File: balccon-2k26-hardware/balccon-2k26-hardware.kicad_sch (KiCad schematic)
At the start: 1 part

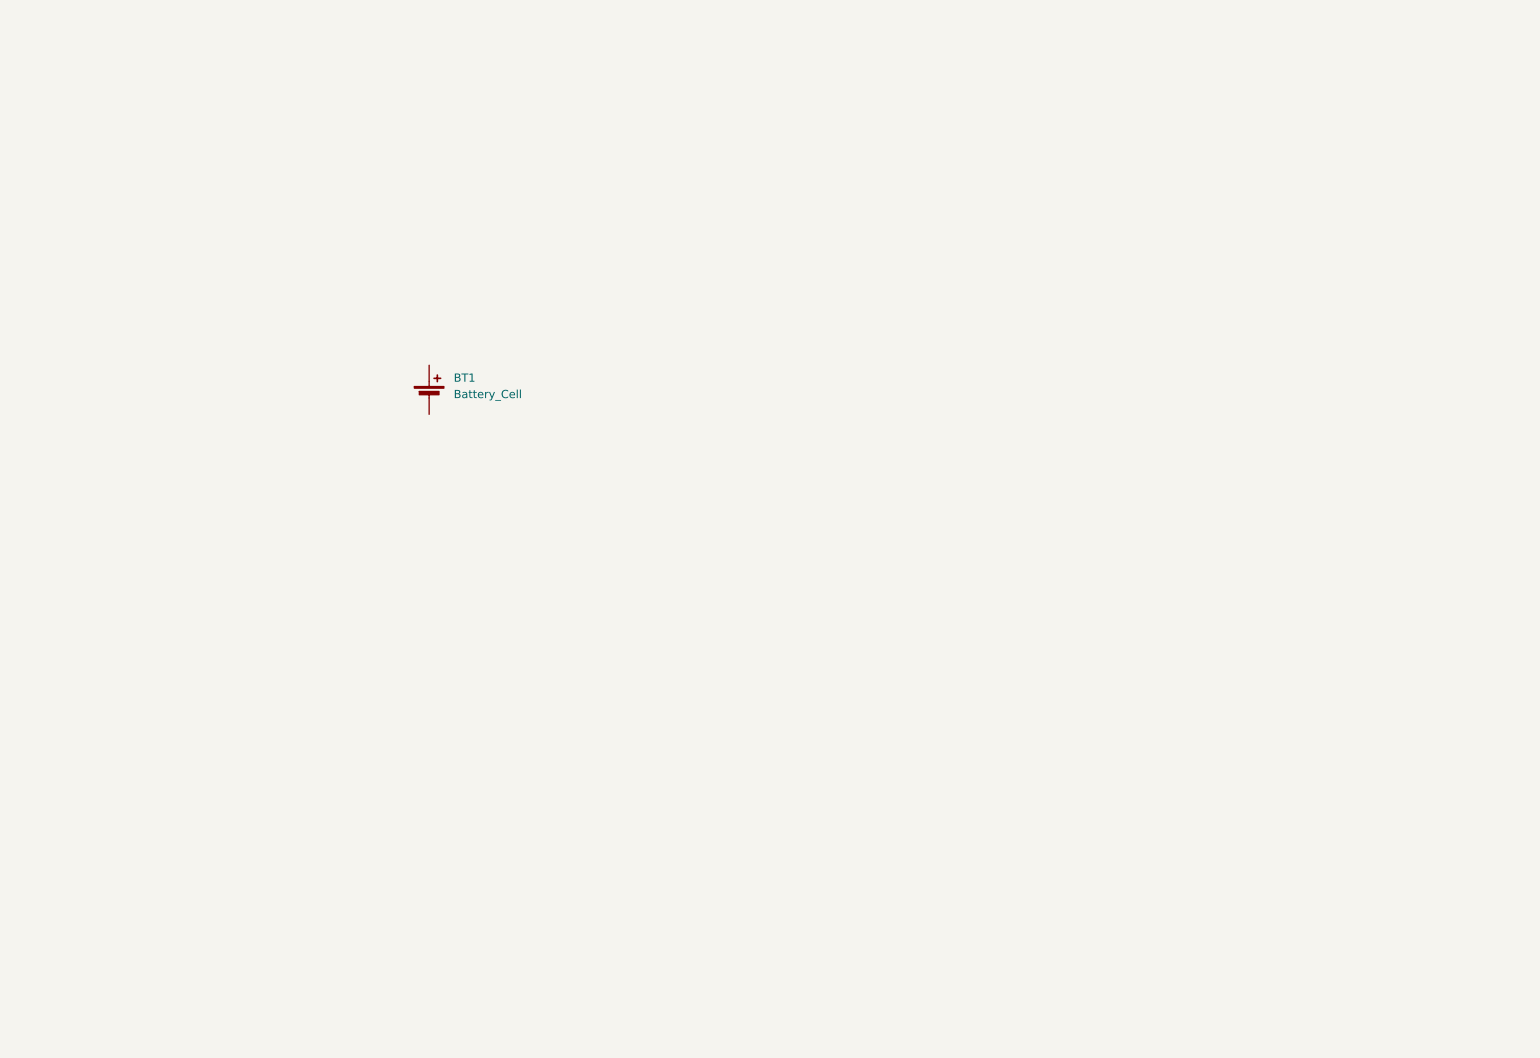
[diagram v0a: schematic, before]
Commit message: Update schematic/board and add hex, log layer exports
Progress the KiCad schematic and board layout, and export the hex and log
layers alongside the existing ones.

Co-Authored-By: Claude Sonnet 5 <noreply@anthropic.com>
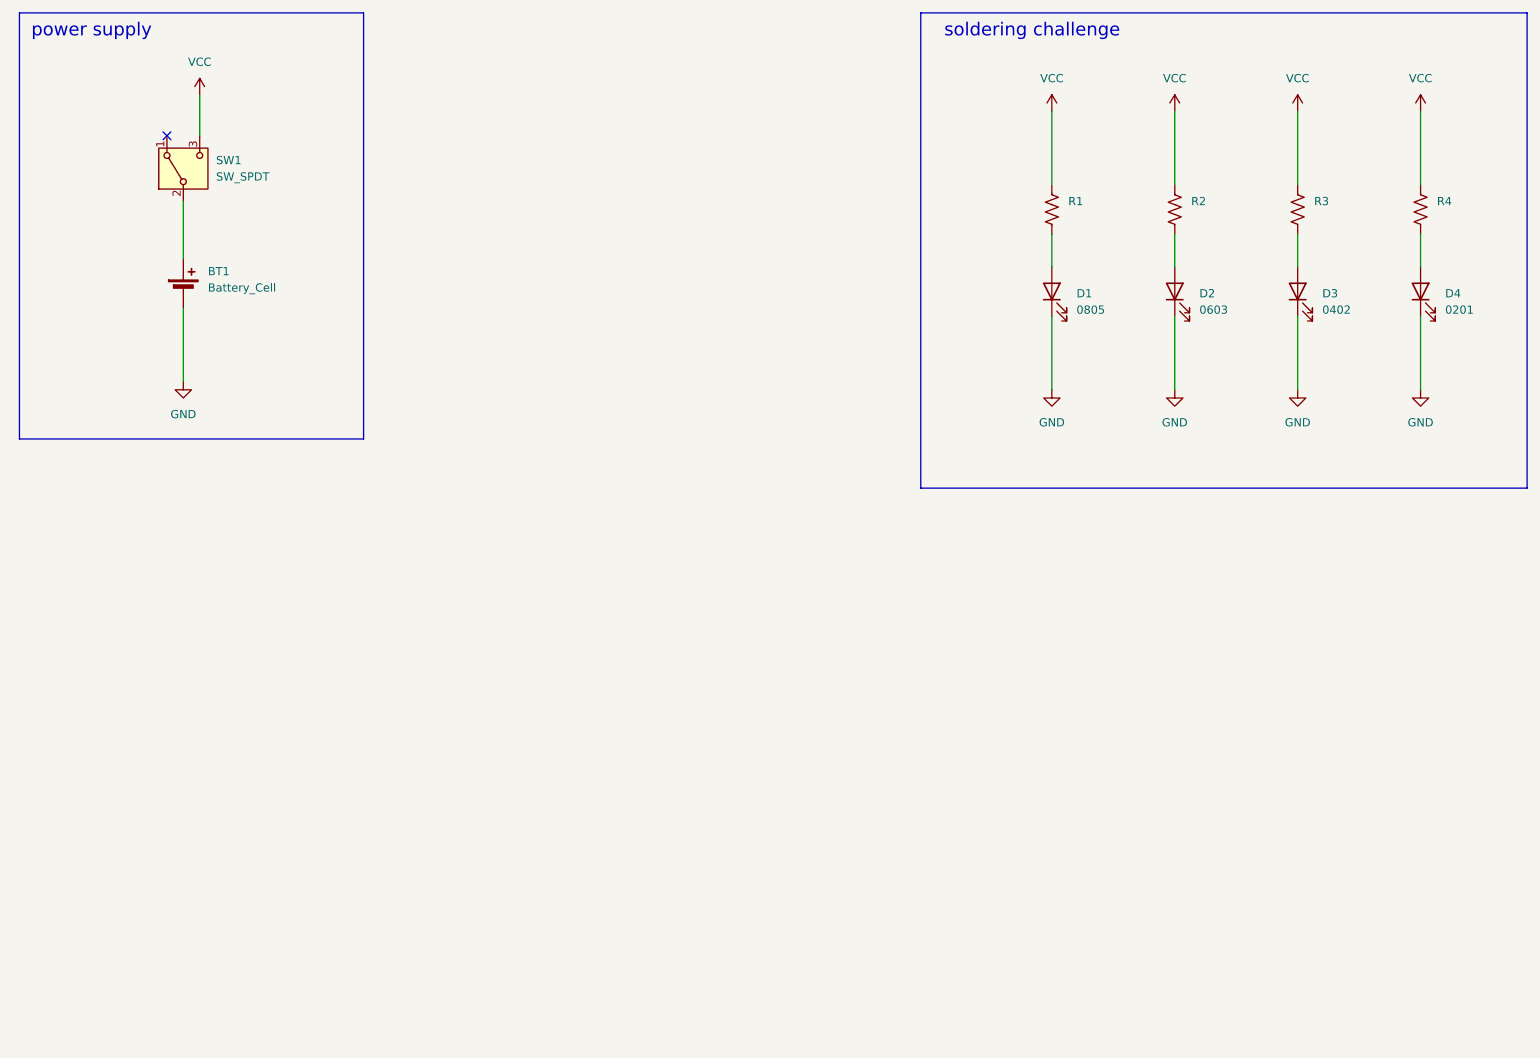
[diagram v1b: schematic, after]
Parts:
- added D1: 0805, LED_SMD:LED_0805_2012Metric_Pad1.15x1.40mm_HandSolder, symbol Device:LED
- added D2: 0603, LED_SMD:LED_0603_1608Metric_Pad1.05x0.95mm_HandSolder, symbol Device:LED
- added D3: 0402, LED_SMD:LED_0402_1005Metric_Pad0.77x0.64mm_HandSolder, symbol Device:LED
- added D4: 0201, LED_SMD:LED_0201_0603Metric_Pad0.64x0.40mm_HandSolder, symbol Device:LED
- added R1, R2, R3, R4: 1k, Resistor_SMD:R_0805_2012Metric_Pad1.20x1.40mm_HandSolder, symbol Device:R_US
- added SW1: SW_SPDT, Button_Switch_SMD:SW_SPDT_PCM12, symbol Switch:SW_SPDT
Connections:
- net at BT1.1 (+): now also SW1.2 (B)
- net GND: now reaches BT1.2 (-)
- net GND: now also D1.1 (K), D2.1 (K), D3.1 (K), D4.1 (K)
- new net: D3.2 (A), R3.2
- new net: D4.2 (A), R4.2
- new net: D1.2 (A), R1.2
- new net: D2.2 (A), R2.2
- new net VCC: R1.1, R2.1, R3.1, R4.1, SW1.3 (C)
- no-connect marks 0 -> 1
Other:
- note added: "power supply"
- note added: "soldering challenge"
- moved on the sheet: BT1

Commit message: Place all components on the board
Update schematic and board layout with full component placement.

Co-Authored-By: Claude Sonnet 5 <noreply@anthropic.com>
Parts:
- added D10, D11, D12, D13, D14, D5, D6, D7, D8, D9: 0805, LED_SMD:LED_0805_2012Metric_Pad1.15x1.40mm_HandSolder, symbol Device:LED
- added R10, R11, R12, R13, R14, R5, R6, R7, R8, R9: 1k, Resistor_SMD:R_0805_2012Metric_Pad1.20x1.40mm_HandSolder, symbol Device:R_US
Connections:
- net GND: now also D10.1 (K), D11.1 (K), D12.1 (K), D13.1 (K), D14.1 (K), D5.1 (K), D6.1 (K), D7.1 (K), D8.1 (K), D9.1 (K)
- net VCC: now also R10.1, R11.1, R12.1, R13.1, R14.1, R5.1, R6.1, R7.1, R8.1, R9.1
- new net: D7.2 (A), R7.2
- new net: D11.2 (A), R11.2
- new net: D12.2 (A), R12.2
- new net: D5.2 (A), R5.2
- new net: D13.2 (A), R13.2
- new net: D6.2 (A), R6.2
- new net: D9.2 (A), R9.2
- new net: D14.2 (A), R14.2
- new net: D8.2 (A), R8.2
- new net: D10.2 (A), R10.2
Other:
- note added: "genelral back lighting"
